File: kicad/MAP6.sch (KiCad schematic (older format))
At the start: 26 parts, among them M1 Motor_vibration, Q1 BC547, SW1 On, U1 LM555

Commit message: big update, added several battery options
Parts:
- added BT2: BAT, map6_fp:cr2032_04_3025-2, symbol map6:BATT_HOLDER
- BT1: footprint map6_fp:cr2032_02 -> map6_fp:cr2032_03
- M1: value Motor_vibration -> Motor
- R1, R2: value 150E -> 220E
- R3: value 15E -> 47E
- R4: value DNP -> 1k; footprint map6_fp:r_0805_DNP -> map6_fp:r_0805
- R6: value DNP -> 10k; footprint map6_fp:r_0805_DNP -> map6_fp:r_0805
- SW1: footprint map6_fp:SW_CuK_JS202011AQN_DPDT_Angled -> map6_fp:SW_SPDT_Straight
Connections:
- net GND: now also BT2.2 (-)
- net at D1.1 (A), D2.1 (A), Q1.3 (E): now also M1.1 (+)
- net at BT1.1 (+), SW1.2 (B): now also BT2.1 (+)
- net at JP1.2 (B), Q1.2 (B), R5.1: no longer M1.1 (+)
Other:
- note added: "Battery Holder\n2x2032 or 2x2016\nwith switch\n\nBT2 is alternate\nfootprint"
- note removed: "Battery Holder\n2x2032 or 2x2016\nwith switch"
- note removed: "NOTE\nWith JUMPER JP1 bridged, output current is variable causing "breathing LED" effect\nC1/R5 values affect breathing effect\n\nWith JUMPER JP1 open, and resistors R4/R6 populated, the 555 works as a classic astable - so output voltage switches between 2/3rd and 1/3rd supply\nC1/R4/R6 values affect astable frequency\n"
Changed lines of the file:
@@
 F 0 "BT1" V 2725 3300 40  0000 L CNN
 F 1 "BAT" V 2800 3300 40  0000 L CNN
-F 2 "map6_fp:cr2032_02" H 2725 3175 60  0001 C CNN
+F 2 "map6_fp:cr2032_03" H 2725 3175 60  0001 C CNN
 F 3 "" H 2725 3175 60  0000 C CNN
 F 4 "HOLDER BATTERY COIN 20MM DIA THM" H 2725 3475 60  0001 L CNN "Field4"
@@
 P 7100 4300
 F 0 "R1" H 7050 4125 40  0000 C CNN
-F 1 "150E" V 7100 4300 40  0000 C CNN
+F 1 "220E" V 7100 4300 40  0000 C CNN
 F 2 "map6_fp:r_0805" V 7030 4300 50  0001 C CNN
 F 3 "" H 7100 4300 50  0000 C CNN
@@
 P 7600 4300
 F 0 "R2" H 7550 4125 40  0000 C CNN
-F 1 "150E" V 7600 4300 40  0000 C CNN
+F 1 "220E" V 7600 4300 40  0000 C CNN
 F 2 "map6_fp:r_0805" V 7530 4300 50  0001 C CNN
 F 3 "" H 7600 4300 50  0000 C CNN
@@
 P 6600 4300
 F 0 "R3" H 6550 4125 40  0000 C CNN
-F 1 "15E" V 6600 4300 40  0000 C CNN
+F 1 "47E" V 6600 4300 40  0000 C CNN
 F 2 "map6_fp:r_0805" V 6530 4300 50  0001 C CNN
 F 3 "" H 6600 4300 50  0000 C CNN
@@
 P 6600 3600
 F 0 "M1" H 6625 3725 50  0000 L CNN
-F 1 "Motor_vibration" V 6500 3725 50  0000 L CNN
+F 1 "Motor" V 6500 3725 50  0001 L CNN
 F 2 "map6_fp:motor_XDCR_C0720B001F" H 6600 3510 50  0001 C CNN
 F 3 "~" H 6600 3510 50  0001 C CNN
@@
 F 0 "SW1" V 2800 2350 40  0000 R CNN
 F 1 "On" V 2725 2350 40  0000 R CNN
-F 2 "map6_fp:SW_CuK_JS202011AQN_DPDT_Angled" H 2725 2475 50  0001 C CNN
+F 2 "map6_fp:SW_SPDT_Straight" H 2725 2475 50  0001 C CNN
 F 3 "~" H 2725 2475 50  0001 C CNN
 	1    2725 2475
@@
 P 4025 2200
 F 0 "R6" H 3975 2025 40  0000 C CNB
-F 1 "DNP" V 4025 2200 40  0000 C CNB
-F 2 "map6_fp:r_0805_DNP" V 3955 2200 50  0001 C CNN
+F 1 "10k" V 4025 2200 40  0000 C CNB
+F 2 "map6_fp:r_0805" V 3955 2200 50  0001 C CNN
 F 3 "" H 4025 2200 50  0000 C CNN
 F 4 "Value" H 4025 2200 60  0001 C CNN "manf#"
@@
 P 4025 1425
 F 0 "R4" H 3975 1250 40  0000 C CNB
-F 1 "DNP" V 4025 1425 40  0000 C CNB
-F 2 "map6_fp:r_0805_DNP" V 3955 1425 50  0001 C CNN
+F 1 "1k" V 4025 1425 40  0000 C CNB
+F 2 "map6_fp:r_0805" V 3955 1425 50  0001 C CNN
 F 3 "" H 4025 1425 50  0000 C CNN
 F 4 "Value" H 4025 1425 60  0001 C CNN "manf#"
@@
 	6175 3775 6175 2825
 Connection ~ 6175 2825
-Wire Wire Line
-	6175 2825 6600 2825
 Wire Wire Line
 	7100 3025 7100 3275
@@
 Wire Notes Line width 10 rgb(255, 128, 0)
 	2200 3450 2200 2200
-Text Notes 2175 2425 2    50   ~ 0
-Battery Holder\n2x2032 or 2x2016\nwith switch
+Text Notes 2175 3450 2    50   ~ 0
+Battery Holder\n2x2032 or 2x2016\nwith switch\n\nBT2 is alternate\nfootprint
 Wire Notes Line width 10 rgb(255, 128, 0)
 	6700 6350 6700 5500
@@
 	4025 3775 4025 4150
 Connection ~ 4025 3025
-Text Notes 2725 5150 0    50   ~ 0
-NOTE\nWith JUMPER JP1 bridged, output current is variable causing "breathing LED" effect\nC1/R5 values affect breathing effect\n\nWith JUMPER JP1 open, and resistors R4/R6 populated, the 555 works as a classic astable - so output voltage switches between 2/3rd and 1/3rd supply\nC1/R4/R6 values affect astable frequency\n
 $Comp
 L map6:BC547 Q1
@@
 STING\nsolder short wire for sting
 Wire Wire Line
-	6600 3400 6600 2825
-Connection ~ 6600 2825
-Wire Wire Line
-	6600 2825 6800 2825
+	6600 3400 6600 3275
+$Comp
+L map6:BATT_HOLDER BT2
+U 1 1 6138C33B
+P 2375 3175
+F 0 "BT2" V 2375 3300 40  0000 L CNN
+F 1 "BAT" V 2450 3300 40  0000 L CNN
+F 2 "map6_fp:cr2032_04_3025-2" H 2375 3175 60  0001 C CNN
+F 3 "" H 2375 3175 60  0000 C CNN
+F 4 "HOLDER BATTERY COIN 20MM DIA THM" H 2375 3475 60  0001 L CNN "Field4"
+F 5 "Coin Cell, Retainer" H 2375 3575 60  0001 L CNN "Field5"
+F 6 "Coin, 20.0mm" H 2375 3675 60  0001 L CNN "Field6"
+F 7 "Keystone Electronics" H 2375 3775 60  0001 L CNN "Field7"
+F 8 "3003" H 2375 3875 60  0001 L CNN "Field8"
+F 9 "Digikey" H 2375 3975 60  0001 L CNN "Field9"
+F 10 "3003K-ND" H 2375 4075 60  0001 L CNN "Field10"
+F 11 "http://www.digikey.com/scripts/DkSearch/dksus.dll?x=0&y=0&lang=en&KeyWords=3003K-ND&cur=USD" H 2375 4175 60  0001 L CNN "Field11"
+	1    2375 3175
+	0    1    1    0
+$EndComp
+Wire Wire Line
+	2375 3375 2725 3375
+Connection ~ 2725 3375
+Wire Wire Line
+	2375 2925 2725 2925
+Connection ~ 2725 2925
+Wire Wire Line
+	7100 3275 6600 3275
+Wire Wire Line
+	6175 2825 6800 2825
 $EndSCHEMATC

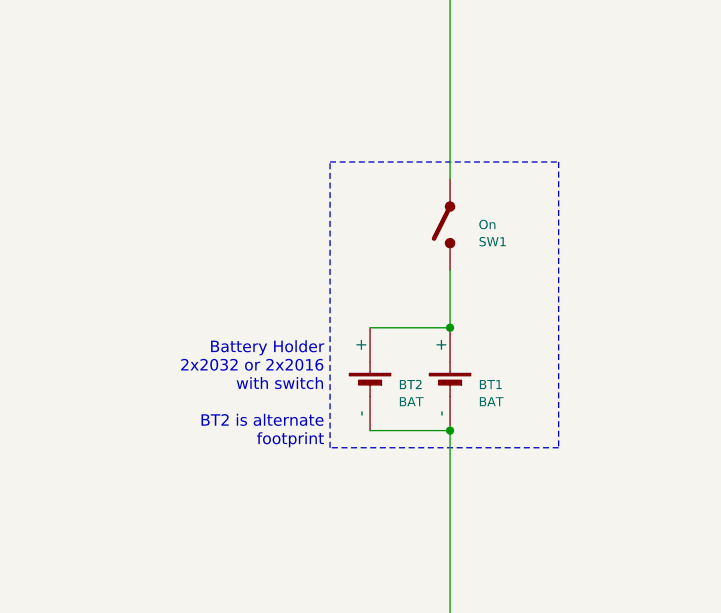
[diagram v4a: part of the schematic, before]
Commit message: another big update after deciding battery options. Ready for FAB
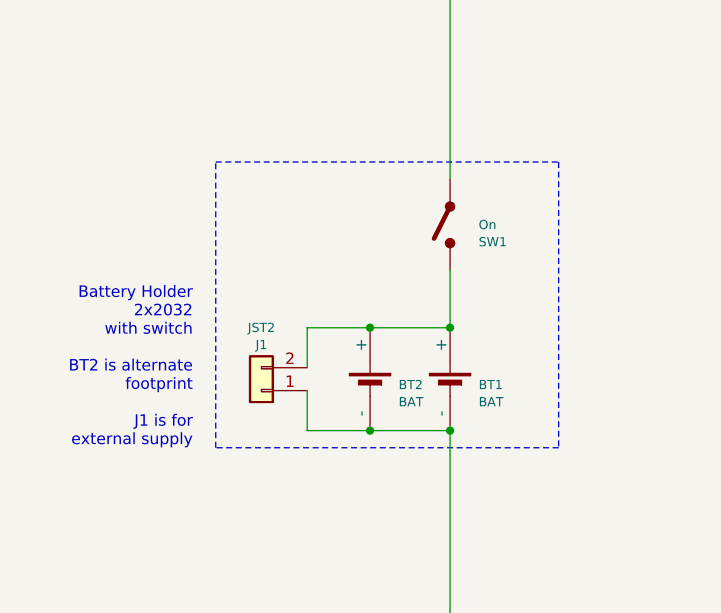
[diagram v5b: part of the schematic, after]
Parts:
- added J1: JST2, map6_fp:JST_EH_B2B-EH-A_1x02_P2.50mm_Vertical, symbol map6:Conn_01x02
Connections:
- net GND: now also J1.1 (Pin_1)
- net at BT1.1 (+), BT2.1 (+), SW1.2 (B): now also J1.2 (Pin_2)
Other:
- note added: "Battery Holder\n2x2032\nwith switch\n\nBT2 is alternate\nfootprint\n\nJ1 is for\nexternal supply"
- note removed: "Battery Holder\n2x2032 or 2x2016\nwith switch\n\nBT2 is alternate\nfootprint"
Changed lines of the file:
@@
 	4025 3025 4025 2450
 Wire Notes Line width 10 rgb(255, 128, 0)
-	2200 2200 3200 2200
+	1700 2200 3200 2200
 Wire Notes Line width 10 rgb(255, 128, 0)
 	3200 2200 3200 3450
 Wire Notes Line width 10 rgb(255, 128, 0)
-	3200 3450 2200 3450
+	3200 3450 1700 3450
 Wire Notes Line width 10 rgb(255, 128, 0)
-	2200 3450 2200 2200
-Text Notes 2175 3450 2    50   ~ 0
-Battery Holder\n2x2032 or 2x2016\nwith switch\n\nBT2 is alternate\nfootprint
+	1700 3450 1700 2200
+Text Notes 1600 3450 2    50   ~ 0
+Battery Holder\n2x2032\nwith switch\n\nBT2 is alternate\nfootprint\n\nJ1 is for\nexternal supply
 Wire Notes Line width 10 rgb(255, 128, 0)
 	6700 6350 6700 5500
@@
 Wire Wire Line
 	6175 2825 6800 2825
+$Comp
+L map6:Conn_01x02 J1
+U 1 1 613AE342
+P 1900 3200
+F 0 "J1" H 1900 3000 40  0000 C CNN
+F 1 "JST2" H 1900 2925 40  0000 C CNN
+F 2 "map6_fp:JST_EH_B2B-EH-A_1x02_P2.50mm_Vertical" H 1900 3200 50  0001 C CNN
+F 3 "~" H 1900 3200 50  0001 C CNN
+	1    1900 3200
+	-1   0    0    1
+$EndComp
+Wire Wire Line
+	2100 2925 2375 2925
+Connection ~ 2375 2925
+Wire Wire Line
+	2100 3200 2100 3375
+Wire Wire Line
+	2100 3375 2375 3375
+Connection ~ 2375 3375
+Wire Wire Line
+	2100 3100 2100 2925
 $EndSCHEMATC
